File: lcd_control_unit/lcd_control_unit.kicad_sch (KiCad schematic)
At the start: 12 parts, among them J1 Conn_01x05_Socket, J2 Conn_01x02_Socket, J3 Conn_01x02_Socket, J4 Conn_01x02_Socket, J5 Conn_01x02_Socket, J6 Conn_01x03_Socket, J7 Conn_01x010_Socket, Q1 2N2222

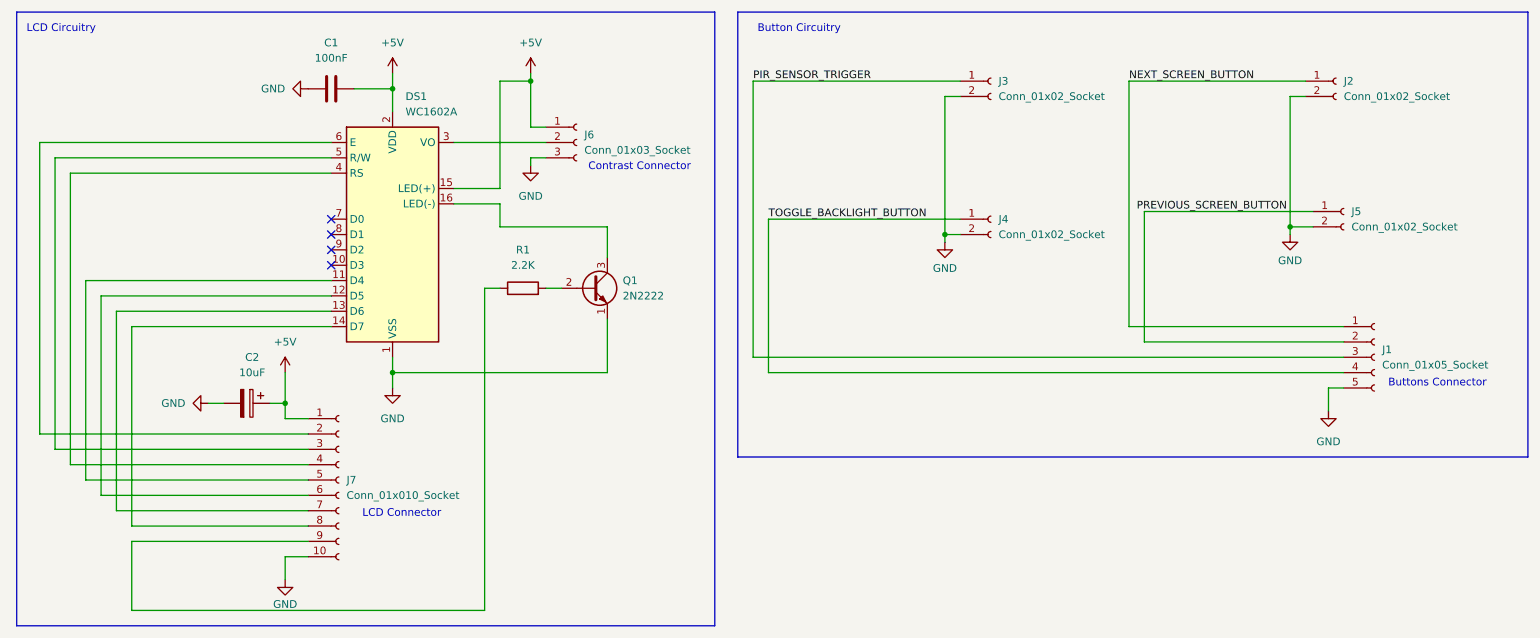
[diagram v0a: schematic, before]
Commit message: fix: ERC errors for LCD Control Unit
Signed-off-by: Scott Gibb <smgibb@yahoo.com>
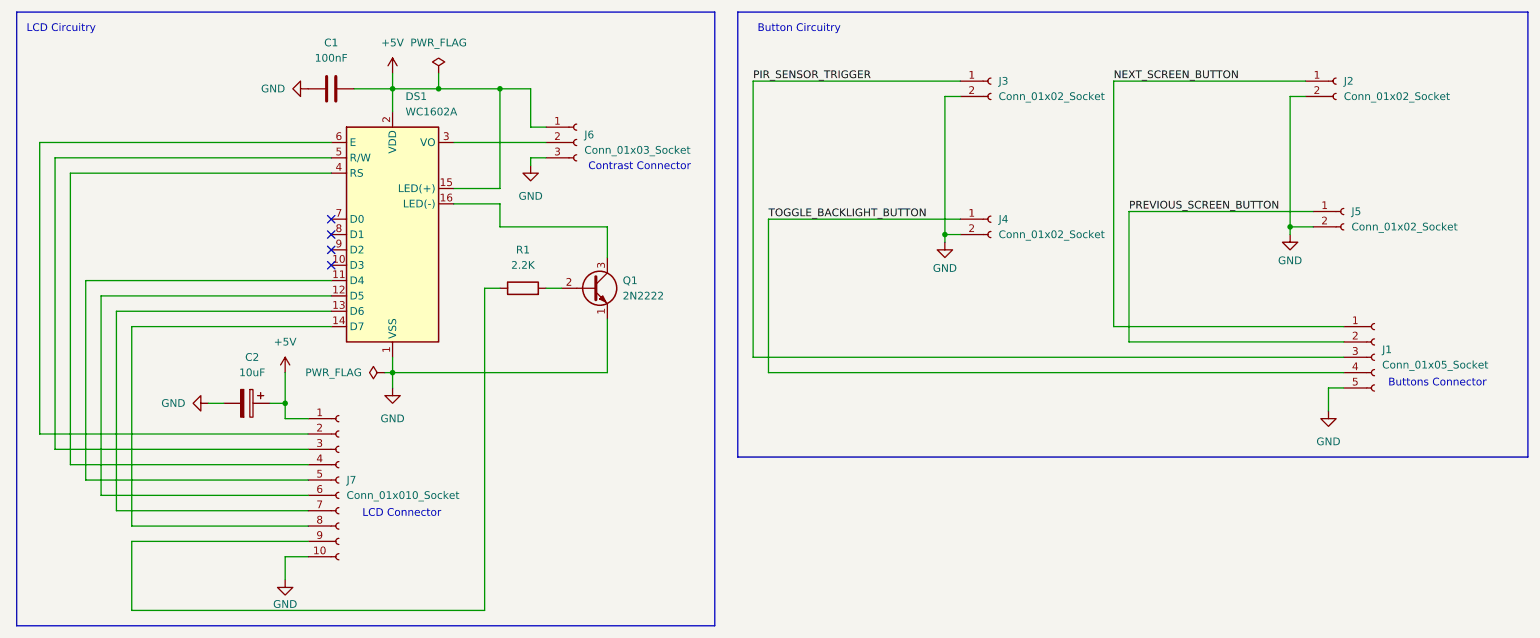
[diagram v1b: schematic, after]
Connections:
- net PREVIOUS_SCREEN_BUTTON: now also J1.2 (Pin_2), J5.1 (Pin_1)
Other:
- title: Control Unit -> LCD Control Unit
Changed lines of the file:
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@@
 	(paper "A4")
 	(title_block
-		(title "Control Unit")
-		(comment 1 "Control Unit Board for Power Monitor Screen")
+		(title "LCD Control Unit")
+		(comment 2 "The board utilises a transistor to turn on and off the backlight of the LCD")
+		(comment 3 "Control Unit Board for Power Monitor Screen")
 	)
 	(rectangle
@@
 	)
 	(junction
-		(at 76.2 26.67)
+		(at 93.98 26.67)
 		(diameter 0)
 		(color 0 0 0 0)
 	)
 	(junction
-		(at 99.06 25.4)
+		(at 76.2 26.67)
 		(diameter 0)
 		(color 0 0 0 0)
@@
 	)
 	(junction
+		(at 83.82 26.67)
+		(diameter 0)
+		(color 0 0 0 0)
+	)
+	(junction
 		(at 58.42 78.74)
 		(diameter 0)
@@
 	(wire
 		(pts
-			(xy 198.12 25.4) (xy 198.12 66.04)
+			(xy 195.58 25.4) (xy 195.58 66.04)
 		)
 		(stroke
@@
 	(wire
 		(pts
-			(xy 200.66 46.99) (xy 200.66 68.58)
+			(xy 198.12 46.99) (xy 198.12 68.58)
 		)
 		(stroke
@@
 	(wire
 		(pts
+			(xy 76.2 26.67) (xy 83.82 26.67)
+		)
+		(stroke
+			(width 0)
+			(type default)
+		)
+	)
+	(wire
+		(pts
 			(xy 170.18 25.4) (xy 135.89 25.4)
 		)
@@
 	(wire
 		(pts
-			(xy 93.98 25.4) (xy 99.06 25.4)
-		)
-		(stroke
-			(width 0)
-			(type default)
-		)
-	)
-	(wire
-		(pts
-			(xy 93.98 25.4) (xy 93.98 43.18)
+			(xy 93.98 26.67) (xy 99.06 26.67)
 		)
 		(stroke
@@
 	(wire
 		(pts
+			(xy 93.98 26.67) (xy 93.98 43.18)
+		)
+		(stroke
+			(width 0)
+			(type default)
+		)
+	)
+	(wire
+		(pts
 			(xy 22.86 88.9) (xy 62.23 88.9)
 		)
@@
 	(wire
 		(pts
+			(xy 83.82 24.13) (xy 83.82 26.67)
+		)
+		(stroke
+			(width 0)
+			(type default)
+		)
+	)
+	(wire
+		(pts
 			(xy 228.6 49.53) (xy 224.79 49.53)
 		)
@@
 	(wire
 		(pts
-			(xy 227.33 25.4) (xy 198.12 25.4)
+			(xy 227.33 25.4) (xy 195.58 25.4)
 		)
 		(stroke
@@
 	(wire
 		(pts
-			(xy 198.12 66.04) (xy 233.68 66.04)
+			(xy 195.58 66.04) (xy 233.68 66.04)
 		)
 		(stroke
@@
 	(wire
 		(pts
+			(xy 74.93 73.66) (xy 76.2 73.66)
+		)
+		(stroke
+			(width 0)
+			(type default)
+		)
+	)
+	(wire
+		(pts
 			(xy 17.78 35.56) (xy 17.78 83.82)
 		)
@@
 	(wire
 		(pts
-			(xy 99.06 24.13) (xy 99.06 25.4)
-		)
-		(stroke
-			(width 0)
-			(type default)
-		)
-	)
-	(wire
-		(pts
-			(xy 200.66 68.58) (xy 233.68 68.58)
+			(xy 198.12 68.58) (xy 233.68 68.58)
 		)
 		(stroke
@@
 	(wire
 		(pts
+			(xy 83.82 26.67) (xy 93.98 26.67)
+		)
+		(stroke
+			(width 0)
+			(type default)
+		)
+	)
+	(wire
+		(pts
 			(xy 138.43 48.26) (xy 170.18 48.26)
 		)
@@
 	(wire
 		(pts
-			(xy 99.06 33.02) (xy 99.06 25.4)
+			(xy 99.06 33.02) (xy 99.06 26.67)
 		)
 		(stroke
@@
 	(wire
 		(pts
-			(xy 228.6 46.99) (xy 200.66 46.99)
+			(xy 228.6 46.99) (xy 198.12 46.99)
 		)
 		(stroke
@@
 	)
 	(label "PREVIOUS_SCREEN_BUTTON"
-		(at 199.39 46.99 0)
+		(at 198.12 46.99 0)
 		(effects
 			(font
@@
 	)
 	(label "NEXT_SCREEN_BUTTON"
-		(at 198.12 25.4 0)
+		(at 195.58 25.4 0)
 		(effects
 			(font
@@
 	)
 	(symbol
+		(lib_id "power:PWR_FLAG")
+		(at 83.82 24.13 0)
+		(unit 1)
+		(body_style 1)
+		(exclude_from_sim no)
+		(in_bom yes)
+		(on_board yes)
+		(in_pos_files yes)
+		(dnp no)
+		(fields_autoplaced yes)
+		(property "Reference" "#FLG01"
+			(at 83.82 22.225 0)
+			(hide yes)
+			(show_name no)
+			(do_not_autoplace no)
+			(effects
+				(font
+					(size 1.27 1.27)
+				)
+			)
+		)
+		(property "Value" "PWR_FLAG"
+			(at 83.82 19.05 0)
+			(show_name no)
+			(do_not_autoplace no)
+			(effects
+				(font
+					(size 1.27 1.27)
+				)
+			)
+		)
+		(property "Footprint" ""
+			(at 83.82 24.13 0)
+			(hide yes)
+			(show_name no)
+			(do_not_autoplace no)
+			(effects
+				(font
+					(size 1.27 1.27)
+				)
+			)
+		)
+		(property "Datasheet" ""
+			(at 83.82 24.13 0)
+			(hide yes)
+			(show_name no)
+			(do_not_autoplace no)
+			(effects
+				(font
+					(size 1.27 1.27)
+				)
+			)
+		)
+		(property "Description" "Special symbol for telling ERC where power comes from"
+			(at 83.82 24.13 0)
+			(hide yes)
+			(show_name no)
+			(do_not_autoplace no)
+			(effects
+				(font
+					(size 1.27 1.27)
+				)
+			)
+		)
+		(pin "1"
+		)
+		(instances
+			(project "lcd_control_unit"
+				(path "/6b50284b-05e1-4845-9c49-b3a0e910d486"
+					(reference "#FLG01")
+					(unit 1)
+				)
+			)
+		)
+	)
+	(symbol
 		(lib_id "Connector:Conn_01x05_Socket")
 		(at 238.76 71.12 0)
@@
 	)
 	(symbol
-		(lib_id "power:+5V")
-		(at 99.06 24.13 0)
-		(unit 1)
-		(body_style 1)
-		(exclude_from_sim no)
-		(in_bom yes)
-		(on_board yes)
-		(in_pos_files yes)
-		(dnp no)
-		(fields_autoplaced yes)
-		(property "Reference" "#PWR02"
-			(at 99.06 27.94 0)
-			(hide yes)
-			(show_name no)
-			(do_not_autoplace no)
-			(effects
-				(font
-					(size 1.27 1.27)
-				)
-			)
-		)
-		(property "Value" "+5V"
-			(at 99.06 19.05 0)
-			(show_name no)
-			(do_not_autoplace no)
-			(effects
-				(font
-					(size 1.27 1.27)
-				)
-			)
-		)
-		(property "Footprint" ""
-			(at 99.06 24.13 0)
-			(hide yes)
-			(show_name no)
-			(do_not_autoplace no)
-			(effects
-				(font
-					(size 1.27 1.27)
-				)
-			)
-		)
-		(property "Datasheet" ""
-			(at 99.06 24.13 0)
-			(hide yes)
-			(show_name no)
-			(do_not_autoplace no)
-			(effects
-				(font
-					(size 1.27 1.27)
-				)
-			)
-		)
-		(property "Description" "Power symbol creates a global label with name \"+5V\""
-			(at 99.06 24.13 0)
-			(hide yes)
-			(show_name no)
-			(do_not_autoplace no)
-			(effects
-				(font
-					(size 1.27 1.27)
-				)
-			)
-		)
-		(pin "1"
-		)
-		(instances
-			(project "lcd_control_unit"
-				(path "/6b50284b-05e1-4845-9c49-b3a0e910d486"
-					(reference "#PWR02")
-					(unit 1)
-				)
-			)
-		)
-	)
-	(symbol
 		(lib_id "power:GND")
 		(at 45.72 78.74 270)
@@
 					(unit 1)
 				)
+			)
+		)
+	)
+	(symbol
+		(lib_id "power:PWR_FLAG")
+		(at 74.93 73.66 90)
+		(unit 1)
+		(body_style 1)
+		(exclude_from_sim no)
+		(in_bom yes)
+		(on_board yes)
+		(in_pos_files yes)
+		(dnp no)
+		(fields_autoplaced yes)
+		(property "Reference" "#FLG02"
+			(at 73.025 73.66 0)
+			(hide yes)
+			(show_name no)
+			(do_not_autoplace no)
+			(effects
+				(font
+					(size 1.27 1.27)
+				)
+			)
+		)
+		(property "Value" "PWR_FLAG"
+			(at 71.12 73.6599 90)
+			(show_name no)
+			(do_not_autoplace no)
+			(effects
+				(font
+					(size 1.27 1.27)
+				)
+				(justify left)
+			)
+		)
+		(property "Footprint" ""
+			(at 74.93 73.66 0)
+			(hide yes)
+			(show_name no)
+			(do_not_autoplace no)
+			(effects
+				(font
+					(size 1.27 1.27)
+				)
+			)
+		)
+		(property "Datasheet" ""
+			(at 74.93 73.66 0)
+			(hide yes)
+			(show_name no)
+			(do_not_autoplace no)
+			(effects
+				(font
+					(size 1.27 1.27)
+				)
+			)
+		)
+		(property "Description" "Special symbol for telling ERC where power comes from"
+			(at 74.93 73.66 0)
+			(hide yes)
+			(show_name no)
+			(do_not_autoplace no)
+			(effects
+				(font
+					(size 1.27 1.27)
+				)
+			)
+		)
+		(pin "1"
+		)
+		(instances
+			(project "lcd_control_unit"
+				(path "/6b50284b-05e1-4845-9c49-b3a0e910d486"
+					(reference "#FLG02")
+					(unit 1)
+				)

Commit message: fix(lcd_control_unit): add powered three-pin PIR connector
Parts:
- J3: value Conn_01x02_Socket -> JST 3P 2.54mm; symbol Connector:Conn_01x02_Socket -> Connector:Conn_01x03_Pin
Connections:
- net +5V: now also J3.1 (Pin_1)
- net GND: now also J3.3 (Pin_3); no longer J3.2 (Pin_2)
- net PIR_SENSOR_TRIGGER: now also J3.2 (Pin_2); no longer J3.1 (Pin_1)
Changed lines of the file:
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@@
-	(symbol
-		(lib_id "Connector:Conn_01x02_Socket")
-		(at 175.26 25.4 0)
-		(unit 1)
-		(body_style 1)
-		(exclude_from_sim no)
-		(in_bom yes)
-		(on_board yes)
-		(in_pos_files yes)
-		(dnp no)
-		(fields_autoplaced yes)
-		(property "Reference" "J3"
-			(at 176.53 25.3999 0)
-			(show_name no)
-			(do_not_autoplace no)
-			(effects
-				(font
-					(size 1.27 1.27)
-				)
-				(justify left)
-			)
-		)
-		(property "Value" "Conn_01x02_Socket"
-			(at 176.53 27.9399 0)
-			(show_name no)
-			(do_not_autoplace no)
-			(effects
-				(font
-					(size 1.27 1.27)
-				)
-				(justify left)
-			)
-		)
-		(property "Footprint" ""
-			(at 175.26 25.4 0)
-			(hide yes)
-			(show_name no)
-			(do_not_autoplace no)
-			(effects
-				(font
-					(size 1.27 1.27)
-				)
-			)
-		)
-		(property "Datasheet" ""
-			(at 175.26 25.4 0)
-			(hide yes)
-			(show_name no)
-			(do_not_autoplace no)
-			(effects
-				(font
-					(size 1.27 1.27)
-				)
-			)
-		)
-		(property "Description" "Generic connector, single row, 01x02, script generated"
-			(at 175.26 25.4 0)
-			(hide yes)
-			(show_name no)
-			(do_not_autoplace no)
-			(effects
-				(font
-					(size 1.27 1.27)
-				)
-			)
-		)
-		(pin "2"
-		)
-		(pin "1"
-		)
-		(instances
-			(project "lcd_control_unit"
-				(path "/6b50284b-05e1-4845-9c49-b3a0e910d486"
-					(reference "J3")
-					(unit 1)
-				)
-			)
-		)
-	)
 	(symbol
 		(lib_id "Connector:Conn_01x02_Socket")
@@
 	)
 	(symbol
+		(lib_id "Connector:Conn_01x03_Pin")
+		(at 175.26 25.4 0)
+		(unit 1)
+		(body_style 1)
+		(exclude_from_sim no)
+		(in_bom yes)
+		(on_board yes)
+		(in_pos_files yes)
+		(dnp no)
+		(property "Reference" "J3"
+			(at 170.18 24.13 0)
+			(show_name no)
+			(do_not_autoplace no)
+			(effects
+				(font
+					(size 1.27 1.27)
+				) (justify right))
+		)
+		(property "Value" "JST 3P 2.54mm"
+			(at 170.18 27.94 0)
+			(show_name no)
+			(do_not_autoplace no)
+			(effects
+				(font
+					(size 1.27 1.27)
+				) (justify right))
+		)
+		(property "Footprint" ""
+			(at 175.26 25.4 0)
+			(hide yes)
+			(show_name no)
+			(do_not_autoplace no)
+			(effects
+				(font
+					(size 1.27 1.27)
+				)
+			)
+		)
+		(property "Datasheet" ""
+			(at 175.26 25.4 0)
+			(hide yes)
+			(show_name no)
+			(do_not_autoplace no)
+			(effects
+				(font
+					(size 1.27 1.27)
+				)
+			)
+		)
+		(property "Description" "JST PIR connector, 2.54mm: pin 1 +5V, pin 2 signal, pin 3 GND"
+			(at 175.26 25.4 0)
+			(hide yes)
+			(show_name no)
+			(do_not_autoplace no)
+			(effects
+				(font
+					(size 1.27 1.27)
+				)
+			)
+		)
+		(pin "1"
+		)
+		(pin "2"
+		)
+		(pin "3"
+		)
+		(instances
+			(project "lcd_control_unit"
+				(path "/6b50284b-05e1-4845-9c49-b3a0e910d486"
+					(reference "J3")
+					(unit 1)
+				)
+			)
+		)
+		(mirror y)
+	)
+	(symbol
 		(lib_id "Connector:Conn_01x02_Socket")
 		(at 175.26 48.26 0)
@@
 		)
 	)
+	(wire
+		(pts
+			(xy 170.18 22.86) (xy 162.56 22.86)
+		)
+		(stroke
+			(width 0)
+			(type default)
+		)
+	)
+	(label "+5V"
+		(at 162.56 22.86 0)
+		(effects
+			(font
+				(size 1.27 1.27)
+			)
+			(justify left bottom)
+		)
+	)
